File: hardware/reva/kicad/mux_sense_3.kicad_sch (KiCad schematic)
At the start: 19 parts

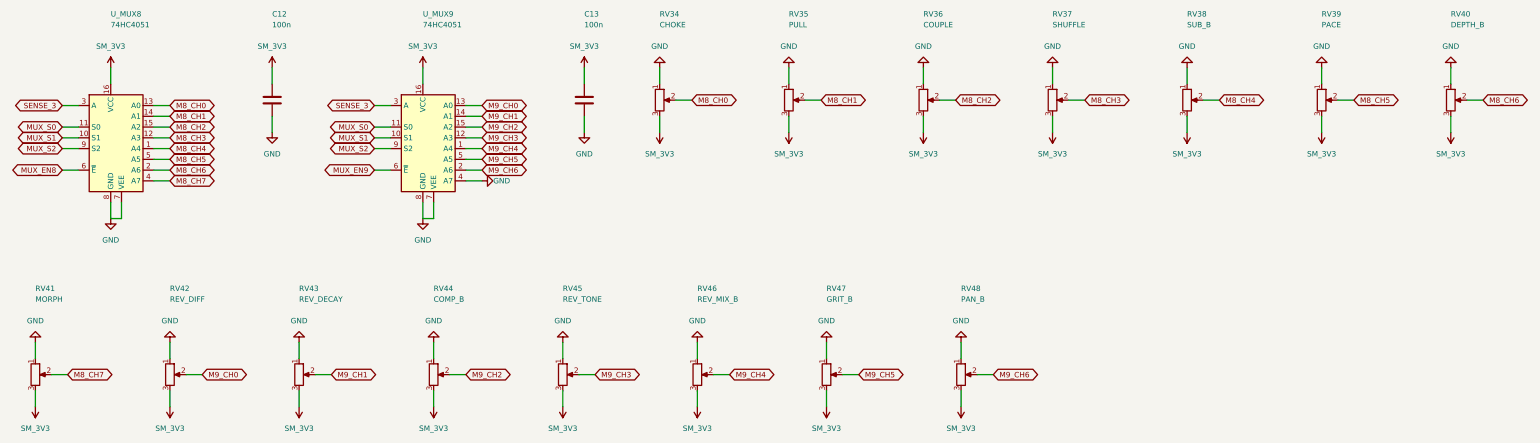
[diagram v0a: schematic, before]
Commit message: feat(reva): 15 LED nets on the 595 chain, four more spare outputs
Spec 2026-10-07 section 5: 15 lamps (LED0..LED14), 73 pots. U_SR4 keeps
LED11..LED14 and gains SR_SPARE8..11, marked no-connect (four more test
points would wrap the chains sheet past the A3 title block). BOMs, review
sheet and the leds / mux sheets regenerated with hardware/reva/build.py.

Co-Authored-By: HAL 9000 <293417720+bea-ton-k@users.noreply.github.com>
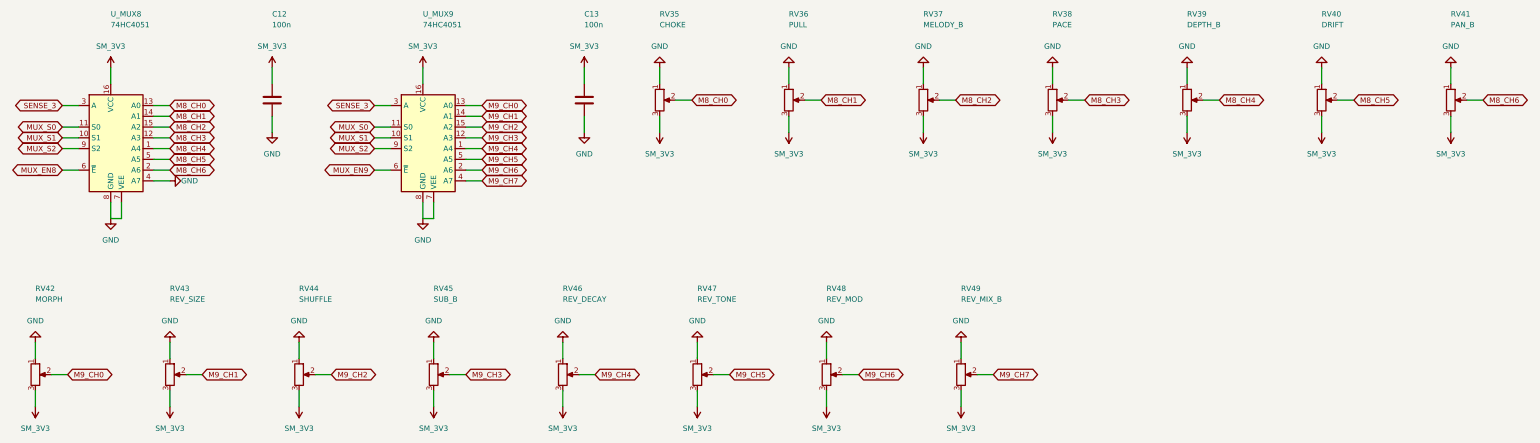
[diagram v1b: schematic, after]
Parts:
- removed RV34: CHOKE, Potentiometer_THT:Potentiometer_Alpha_RD901F-40-00D_Single_Vertical, symbol Device:R_Potentiometer
- added RV49: REV_MIX_B, Potentiometer_THT:Potentiometer_Alpha_RD901F-40-00D_Single_Vertical, symbol Device:R_Potentiometer
- RV35: value PULL -> CHOKE; PanelId PULL -> CHOKE
- RV36: value COUPLE -> PULL; PanelId COUPLE -> PULL
- RV37: value SHUFFLE -> MELODY_B; PanelId SHUFFLE -> MELODY_B
- RV38: value SUB_B -> PACE; PanelId SUB_B -> PACE
- RV39: value PACE -> DEPTH_B; PanelId PACE -> DEPTH_B
- RV40: value DEPTH_B -> DRIFT; PanelId DEPTH_B -> DRIFT
- RV41: value MORPH -> PAN_B; PanelId MORPH -> PAN_B
- RV42: value REV_DIFF -> MORPH; PanelId REV_DIFF -> MORPH
- RV43: value REV_DECAY -> REV_SIZE; PanelId REV_DECAY -> REV_SIZE
- RV44: value COMP_B -> SHUFFLE; PanelId COMP_B -> SHUFFLE
- RV45: value REV_TONE -> SUB_B; PanelId REV_TONE -> SUB_B
- RV46: value REV_MIX_B -> REV_DECAY; PanelId REV_MIX_B -> REV_DECAY
- RV47: value GRIT_B -> REV_TONE; PanelId GRIT_B -> REV_TONE
- RV48: value PAN_B -> REV_MOD; PanelId PAN_B -> REV_MOD
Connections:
- net GND: now also U_MUX8.4 (A7), RV49.1; no longer U_MUX9.4 (A7)
- net M8_CH0: now also RV35.2
- net M8_CH1: now also RV36.2; no longer RV35.2
- net M8_CH2: now also RV37.2; no longer RV36.2
- net M8_CH3: now also RV38.2; no longer RV37.2
- net M8_CH4: now also RV39.2; no longer RV38.2
- net M8_CH5: now also RV40.2; no longer RV39.2
- net M8_CH6: now also RV41.2; no longer RV40.2
- net SM_3V3: now also RV49.3
- removed net M8_CH7: RV41.2, U_MUX8.4 (A7)
- new net M9_CH7: RV49.2, U_MUX9.4 (A7)
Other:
- moved on the sheet: RV35, RV36, RV37, RV38, RV39, RV40, RV41, RV42, RV43, RV44, RV45, RV46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

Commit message: chore(reva): panel map and schematic follow the 23.0 centre pitch
assign.py and build.py re-run on the new hole list. The split and the
band counts are unchanged: one split at x = 213.00 (MELODY_B in
SENSE_3's band, the rest of that column in SENSE_1's); bands 20 + 2
calibration / 14 / 15 / 24 pots, 5 spare channels. Inside SENSE_3 nine
centre/deck-B pots change mux channel (the centre columns moved), and
the LED chain swaps SONG_A_L (now index 1) and GATE_A_L (index 2):
SONG's lamp moved down beside its word. Farthest pot from its mux
group's centre: SENSE_2 28.5 -> 27.7 mm, SENSE_3 39.2 -> 36.8 mm.

Co-Authored-By: HAL 9000 <293417720+bea-ton-k@users.noreply.github.com>
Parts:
- RV38: value PACE -> MORPH; PanelId PACE -> MORPH
- RV39: value DEPTH_B -> PACE; PanelId DEPTH_B -> PACE
- RV40: value DRIFT -> DEPTH_B; PanelId DRIFT -> DEPTH_B
- RV41: value PAN_B -> SUB_B; PanelId PAN_B -> SUB_B
- RV42: value MORPH -> REV_SIZE; PanelId MORPH -> REV_SIZE
- RV43: value REV_SIZE -> SHUFFLE; PanelId REV_SIZE -> SHUFFLE
- RV44: value SHUFFLE -> REV_DECAY; PanelId SHUFFLE -> REV_DECAY
- RV45: value SUB_B -> DRIFT; PanelId SUB_B -> DRIFT
- RV46: value REV_DECAY -> PAN_B; PanelId REV_DECAY -> PAN_B
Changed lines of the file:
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@@
 			(at 262.89 19.05 0)
 			(effects (font (size 1.27 1.27)) (justify left)))
-		(property "Value" "PACE"
+		(property "Value" "MORPH"
 			(at 262.89 21.59 0)
 			(effects (font (size 1.27 1.27)) (justify left)))
@@
 			(at 262.89 39.37 0)
 			(effects (font (size 1.27 1.27)) (justify left) (hide yes)))
-		(property "PanelId" "PACE"
+		(property "PanelId" "MORPH"
 			(at 262.89 39.37 0)
 			(effects (font (size 1.27 1.27)) (justify left) (hide yes)))
@@
 			(at 294.64 19.05 0)
 			(effects (font (size 1.27 1.27)) (justify left)))
-		(property "Value" "DEPTH_B"
+		(property "Value" "PACE"
 			(at 294.64 21.59 0)
 			(effects (font (size 1.27 1.27)) (justify left)))
@@
 			(at 294.64 39.37 0)
 			(effects (font (size 1.27 1.27)) (justify left) (hide yes)))
-		(property "PanelId" "DEPTH_B"
+		(property "PanelId" "PACE"
 			(at 294.64 39.37 0)
 			(effects (font (size 1.27 1.27)) (justify left) (hide yes)))
@@
 			(at 326.39 19.05 0)
 			(effects (font (size 1.27 1.27)) (justify left)))
-		(property "Value" "DRIFT"
+		(property "Value" "DEPTH_B"
 			(at 326.39 21.59 0)
 			(effects (font (size 1.27 1.27)) (justify left)))
@@
 			(at 326.39 39.37 0)
 			(effects (font (size 1.27 1.27)) (justify left) (hide yes)))
-		(property "PanelId" "DRIFT"
+		(property "PanelId" "DEPTH_B"
 			(at 326.39 39.37 0)
 			(effects (font (size 1.27 1.27)) (justify left) (hide yes)))
@@
 			(at 356.87 19.05 0)
 			(effects (font (size 1.27 1.27)) (justify left)))
-		(property "Value" "PAN_B"
+		(property "Value" "SUB_B"
 			(at 356.87 21.59 0)
 			(effects (font (size 1.27 1.27)) (justify left)))
@@
 			(at 356.87 39.37 0)
 			(effects (font (size 1.27 1.27)) (justify left) (hide yes)))
-		(property "PanelId" "PAN_B"
+		(property "PanelId" "SUB_B"
 			(at 356.87 39.37 0)
 			(effects (font (size 1.27 1.27)) (justify left) (hide yes)))
@@
 			(at 22.86 83.82 0)
 			(effects (font (size 1.27 1.27)) (justify left)))
-		(property "Value" "MORPH"
+		(property "Value" "REV_SIZE"
 			(at 22.86 86.36 0)
 			(effects (font (size 1.27 1.27)) (justify left)))
@@
 			(at 22.86 104.14 0)
 			(effects (font (size 1.27 1.27)) (justify left) (hide yes)))
-		(property "PanelId" "MORPH"
+		(property "PanelId" "REV_SIZE"
 			(at 22.86 104.14 0)
 			(effects (font (size 1.27 1.27)) (justify left) (hide yes)))
@@
 			(at 54.61 83.82 0)
 			(effects (font (size 1.27 1.27)) (justify left)))
-		(property "Value" "REV_SIZE"
+		(property "Value" "SHUFFLE"
 			(at 54.61 86.36 0)
 			(effects (font (size 1.27 1.27)) (justify left)))
@@
 			(at 54.61 104.14 0)
 			(effects (font (size 1.27 1.27)) (justify left) (hide yes)))
-		(property "PanelId" "REV_SIZE"
+		(property "PanelId" "SHUFFLE"
 			(at 54.61 104.14 0)
 			(effects (font (size 1.27 1.27)) (justify left) (hide yes)))
@@
 			(at 85.09 83.82 0)
 			(effects (font (size 1.27 1.27)) (justify left)))
-		(property "Value" "SHUFFLE"
+		(property "Value" "REV_DECAY"
 			(at 85.09 86.36 0)
 			(effects (font (size 1.27 1.27)) (justify left)))
@@
 			(at 85.09 104.14 0)
 			(effects (font (size 1.27 1.27)) (justify left) (hide yes)))
-		(property "PanelId" "SHUFFLE"
+		(property "PanelId" "REV_DECAY"
 			(at 85.09 104.14 0)
 			(effects (font (size 1.27 1.27)) (justify left) (hide yes)))
@@
 			(at 116.84 83.82 0)
 			(effects (font (size 1.27 1.27)) (justify left)))
-		(property "Value" "SUB_B"
+		(property "Value" "DRIFT"
 			(at 116.84 86.36 0)
 			(effects (font (size 1.27 1.27)) (justify left)))
@@
 			(at 116.84 104.14 0)
 			(effects (font (size 1.27 1.27)) (justify left) (hide yes)))
-		(property "PanelId" "SUB_B"
+		(property "PanelId" "DRIFT"
 			(at 116.84 104.14 0)
 			(effects (font (size 1.27 1.27)) (justify left) (hide yes)))
@@
 			(at 147.32 83.82 0)
 			(effects (font (size 1.27 1.27)) (justify left)))
-		(property "Value" "REV_DECAY"
+		(property "Value" "PAN_B"
 			(at 147.32 86.36 0)
 			(effects (font (size 1.27 1.27)) (justify left)))
@@
 			(at 147.32 104.14 0)
 			(effects (font (size 1.27 1.27)) (justify left) (hide yes)))
-		(property "PanelId" "REV_DECAY"
+		(property "PanelId" "PAN_B"
 			(at 147.32 104.14 0)
 			(effects (font (size 1.27 1.27)) (justify left) (hide yes)))
